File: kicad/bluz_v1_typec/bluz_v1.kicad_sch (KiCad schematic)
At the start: 73 parts, among them J10 Conn, J11 Conn, J12 BTAnt, J2 Conn, J3 Conn, J4 Conn, J5 Conn, J6 Conn, J7 Conn, J8 Conn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

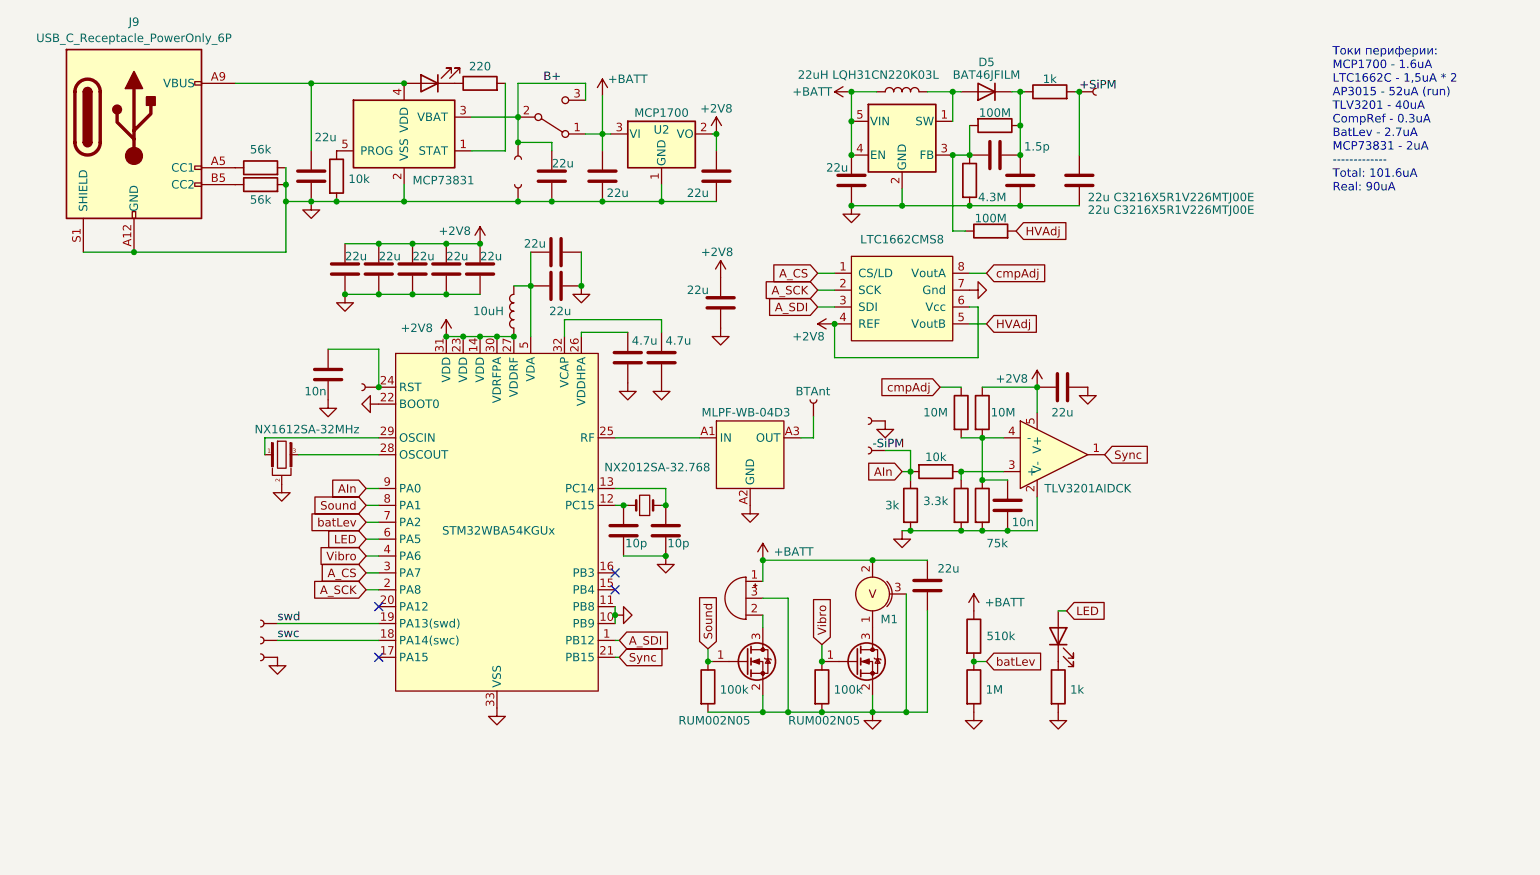
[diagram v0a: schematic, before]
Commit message: удалено:       kicad/bluz_v1_typec/bluz_v1-backups/bluz_v1-2024-12-26_190152.zip 	удалено:       kicad/bluz_v1_typec/bluz_v1-backups/bluz_v1-2024-12-27_152005.zip 	удалено:       kicad/bluz_v1_typec/bluz_v1-backups/bluz_v1-2025-01-20_122513.zip 	удалено:       kicad/bluz_v1_typec/bluz_v1-backups/bluz_v1-2025-01-21_100500.zip 	удалено:       kicad/bluz_v1_typec/bluz_v1-backups/bluz_v1-2025-01-21_105512.zip 	удалено:       kicad/bluz_v1_typec/bluz_v1-backups/bluz_v1-2025-01-21_110513.zip 	изменено:      kicad/bluz_v1_typec/bluz_v1.kicad_pcb 	изменено:      kicad/bluz_v1_typec/bluz_v1.kicad_pro 	изменено:      kicad/bluz_v1_typec/bluz_v1.kicad_sch 	изменено:      kicad/bluz_v1_typec/fp-info-cache
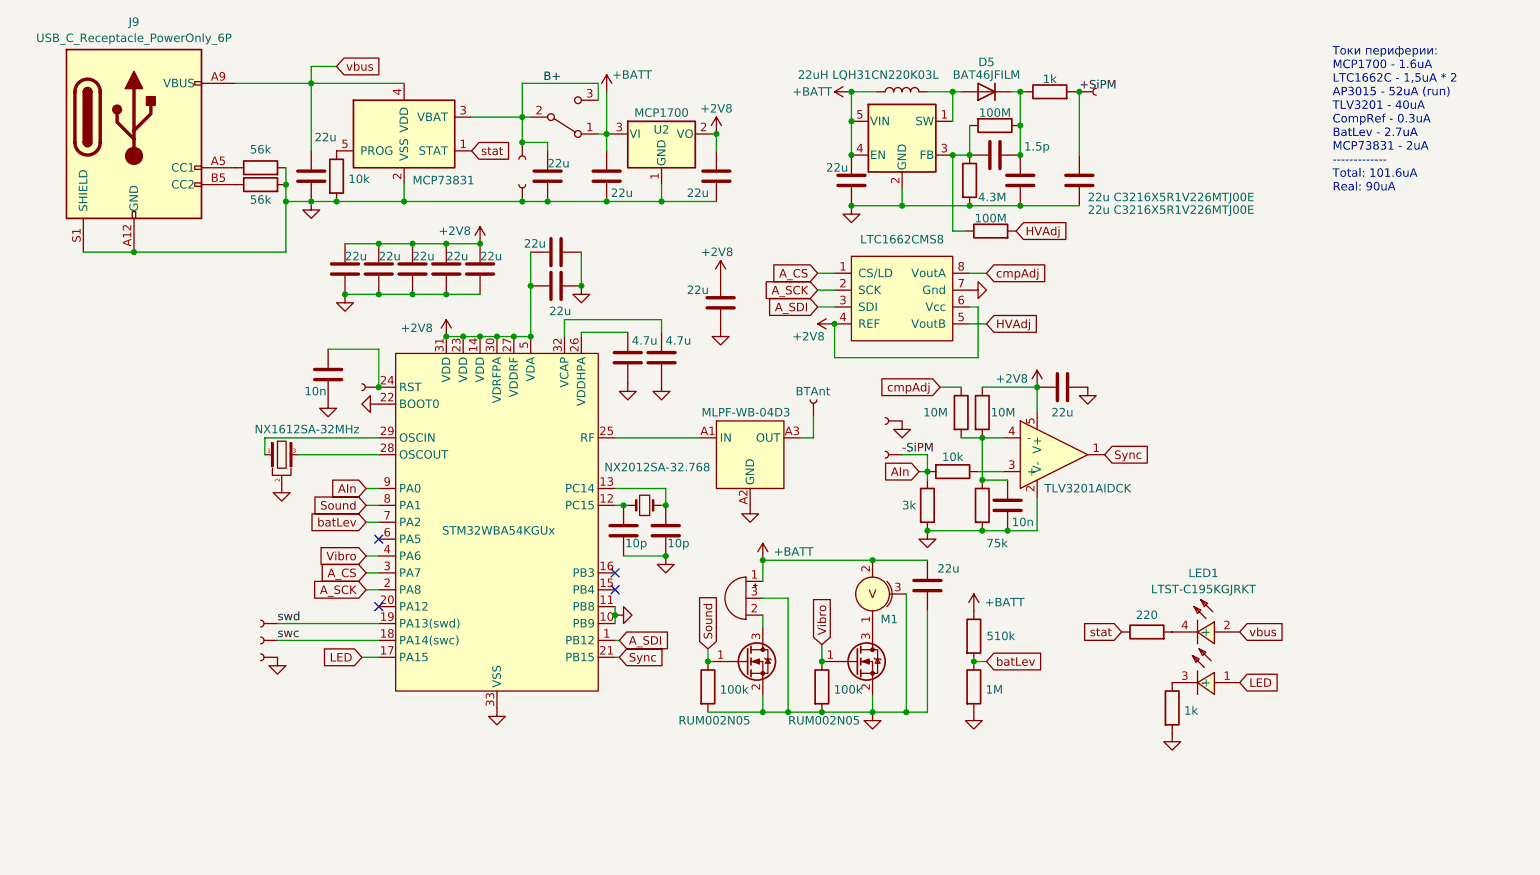
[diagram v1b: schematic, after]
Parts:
- removed D2: Red, LED_SMD:LED_0402_1005Metric, symbol Device:LED
- removed D3: Green, LED_SMD:LED_0402_1005Metric, symbol Device:LED
- removed L1: 10uH, Inductor_SMD:L_0603_1608Metric, symbol Device:L
- removed R*1: 3.3k, Resistor_SMD:R_0201_0603Metric, symbol Device:R
- added LED1: LTST-C195KGJRKT, easyeda2kicad:LED-ARRAY-SMD_0603-4P-L1.6-W1.5-BR-RD, symbol easyeda2kicad:LTST-C195KGJRKT
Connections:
- net +2V8: now also C23.1, C8.1, D1.5 (VDA)
- net LED: now also D1.17 (PA15), LED1.1 (+); no longer D1.6 (PA5)
- net stat: now reaches R4.1
- net stat: now also U1.1 (STAT)
- net at R4.2: now also LED1.4 (-); no longer U1.1 (STAT)
- net vbus: now reaches C4.1, J9.A9 (VBUS), J9.B9 (VBUS), U1.4 (VDD)
- net vbus: now also LED1.2 (+)
- net at R5.1: now also LED1.3 (-)

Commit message: удалено:       kicad/bluz_v1_typec/bluz_v1-backups/bluz_v1-2025-01-22_110710.zip 	удалено:       kicad/bluz_v1_typec/bluz_v1-backups/bluz_v1-2025-01-28_102500.zip 	удалено:       kicad/bluz_v1_typec/bluz_v1-backups/bluz_v1-2025-01-28_134021.zip 	удалено:       kicad/bluz_v1_typec/bluz_v1-backups/bluz_v1-2025-02-11_170038.zip 	удалено:       kicad/bluz_v1_typec/bluz_v1-backups/bluz_v1-2025-02-25_125512.zip 	изменено:      kicad/bluz_v1_typec/bluz_v1.kicad_pcb 	изменено:      kicad/bluz_v1_typec/bluz_v1.kicad_prl 	изменено:      kicad/bluz_v1_typec/bluz_v1.kicad_pro 	изменено:      kicad/bluz_v1_typec/bluz_v1.kicad_sch 	изменено:      kicad/bluz_v1_typec/fp-info-cache 	изменено:      kicad/bluz_v1_typec/gerber/BluZ.zip 	удалено:       kicad/bluz_v1_typec/gerber/bluz_v1-job.gbrjob 	изменено:      kicad/bluz_v1_typec/gerber/mk-gerber.sh 	изменено:      kicad/bluz_v1_typec/gerber/mk-gerber.sh~
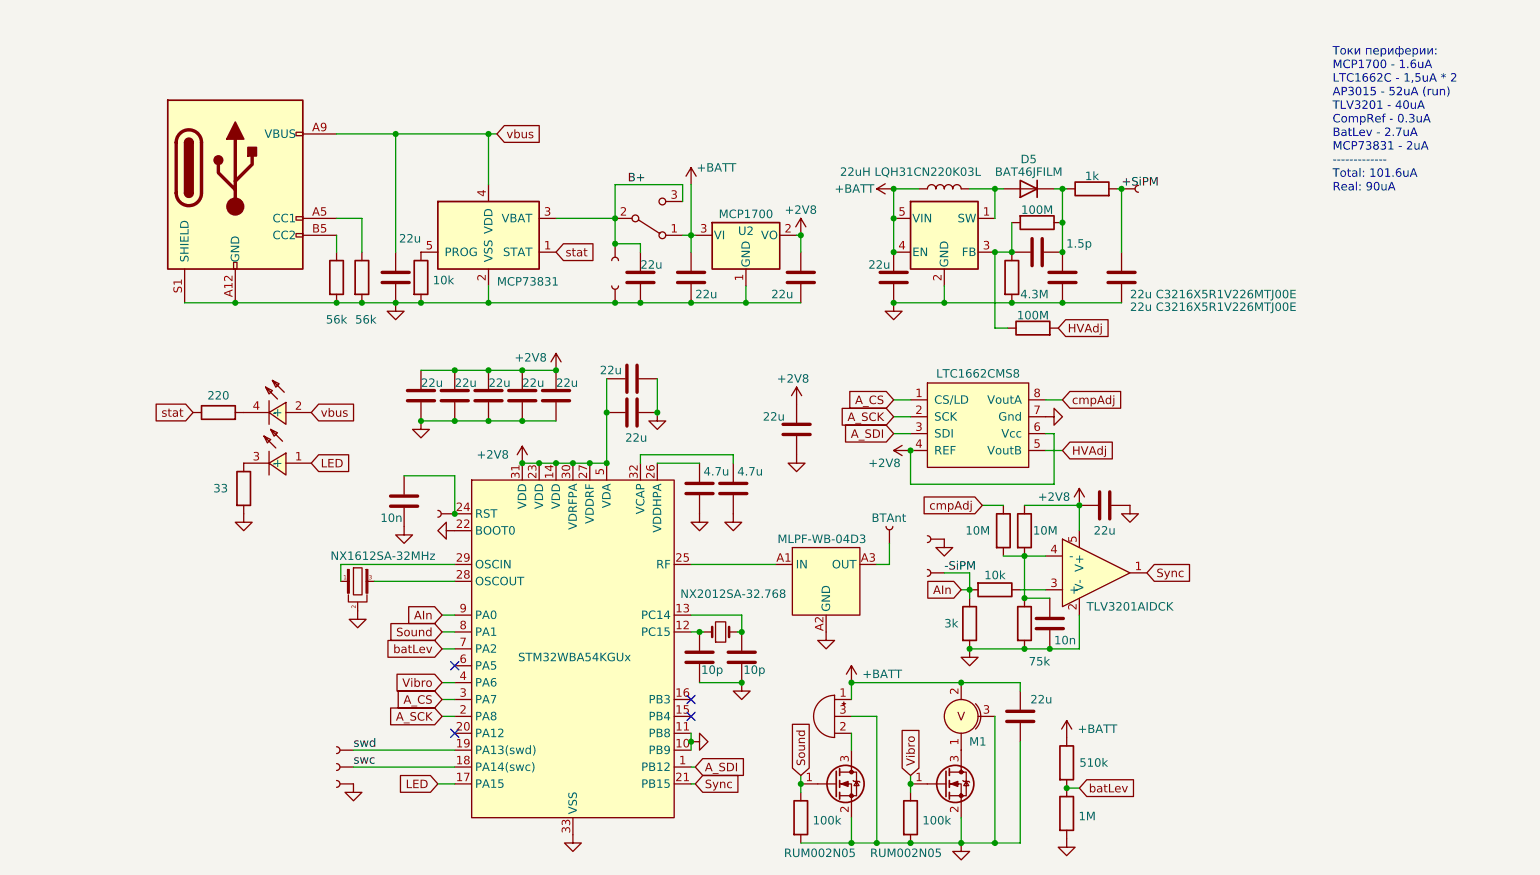
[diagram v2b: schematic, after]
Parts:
- removed BZ1: Buzzer, My-library:Buzzer55x55, symbol Device:Buzzer
- added BZ1: Buzzer, lib:Buzzer55x55, symbol My_Library:Buzzer
- R5: value 1k -> 33
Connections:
- net +BATT: now also BZ1.1 (-)
- net GND: now also BZ1.3 (GND)
- net at Q1.3 (D): now also BZ1.2 (+)
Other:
- moved on the sheet: D5, M1, U2

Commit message: удалено:       kicad/bluz_v1_typec/bluz_v1-backups/bluz_v1-2025-03-25_124207.zip 	удалено:       kicad/bluz_v1_typec/bluz_v1-backups/bluz_v1-2025-03-25_145630.zip 	изменено:      kicad/bluz_v1_typec/bluz_v1.kicad_pcb 	изменено:      kicad/bluz_v1_typec/bluz_v1.kicad_prl 	изменено:      kicad/bluz_v1_typec/bluz_v1.kicad_sch
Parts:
- R17, R18: value 56k -> 5.1k
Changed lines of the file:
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@@
 	(wire
 		(pts
-			(xy 69.85 125.73) (xy 85.09 125.73)
+			(xy 73.66 125.73) (xy 85.09 125.73)
 		)
 		(stroke
@@
 	(wire
 		(pts
-			(xy 82.55 128.27) (xy 85.09 128.27)
+			(xy 83.82 128.27) (xy 85.09 128.27)
 		)
 		(stroke
@@
 	(wire
 		(pts
-			(xy 69.85 123.19) (xy 85.09 123.19)
+			(xy 73.66 123.19) (xy 85.09 123.19)
 		)
 		(stroke
@@
 	(wire
 		(pts
-			(xy 83.185 107.95) (xy 85.09 107.95)
+			(xy 83.82 107.95) (xy 85.09 107.95)
 		)
 		(stroke
@@
 	(wire
 		(pts
-			(xy 83.185 102.87) (xy 85.09 102.87)
+			(xy 83.82 102.87) (xy 85.09 102.87)
 		)
 		(stroke
@@
 	(wire
 		(pts
-			(xy 83.185 118.11) (xy 85.09 118.11)
+			(xy 83.82 118.11) (xy 85.09 118.11)
 		)
 		(stroke
@@
 	(wire
 		(pts
-			(xy 83.185 113.03) (xy 85.09 113.03)
+			(xy 83.82 113.03) (xy 85.09 113.03)
 		)
 		(stroke
@@
 	(wire
 		(pts
-			(xy 83.185 115.57) (xy 85.09 115.57)
+			(xy 83.82 115.57) (xy 85.09 115.57)
 		)
 		(stroke
@@
 	(wire
 		(pts
-			(xy 83.185 105.41) (xy 85.09 105.41)
+			(xy 83.82 105.41) (xy 85.09 105.41)
 		)
 		(stroke
@@
 	)
 	(label "swd"
-		(at 69.85 123.19 0)
+		(at 73.66 123.19 0)
 		(effects
 			(font
@@
 	)
 	(label "swc"
-		(at 69.85 125.73 0)
+		(at 73.66 125.73 0)
 		(effects
 			(font
@@
 	(global_label "Vibro"
 		(shape input)
-		(at 83.185 113.03 180)
+		(at 83.82 113.03 180)
 		(fields_autoplaced yes)
 		(effects
@@
 		)
 		(property "Intersheetrefs" "${INTERSHEET_REFS}"
-			(at 75.9943 113.1094 0)
+			(at 76.6293 113.1094 0)
 			(effects
 				(font
@@
 	(global_label "A_SCK"
 		(shape input)
-		(at 83.185 118.11 180)
+		(at 83.82 118.11 180)
 		(fields_autoplaced yes)
 		(effects
@@
 		)
 		(property "Intersheetrefs" "${INTERSHEET_REFS}"
-			(at 74.9662 118.0306 0)
+			(at 75.6012 118.0306 0)
 			(effects
 				(font
@@
 	(global_label "AIn"
 		(shape input)
-		(at 83.185 102.87 180)
+		(at 83.82 102.87 180)
 		(fields_autoplaced yes)
 		(effects
@@
 		)
 		(property "Intersheetrefs" "${INTERSHEET_REFS}"
-			(at 77.9295 102.9494 0)
+			(at 78.5645 102.9494 0)
 			(effects
 				(font
@@
 	(global_label "Sound"
 		(shape input)
-		(at 83.185 105.41 180)
+		(at 83.82 105.41 180)
 		(fields_autoplaced yes)
 		(effects
@@
 		)
 		(property "Intersheetrefs" "${INTERSHEET_REFS}"
-			(at 74.9662 105.3306 0)
+			(at 75.6012 105.3306 0)
 			(effects
 				(font
@@
 	(global_label "A_CS"
 		(shape input)
-		(at 83.185 115.57 180)
+		(at 83.82 115.57 180)
 		(fields_autoplaced yes)
 		(effects
@@
 		)
 		(property "Intersheetrefs" "${INTERSHEET_REFS}"
-			(at 76.2362 115.4906 0)
+			(at 76.8712 115.4906 0)
 			(effects
 				(font
@@
 	(global_label "batLev"
 		(shape input)
-		(at 83.185 107.95 180)
+		(at 83.82 107.95 180)
 		(fields_autoplaced yes)
 		(effects
@@
 		)
 		(property "Intersheetrefs" "${INTERSHEET_REFS}"
-			(at 74.6638 108.0294 0)
+			(at 75.2988 108.0294 0)
 			(effects
 				(font
@@
 	(global_label "LED"
 		(shape input)
-		(at 82.55 128.27 180)
+		(at 83.82 128.27 180)
 		(fields_autoplaced yes)
 		(effects
@@
 		)
 		(property "Intersheetrefs" "${INTERSHEET_REFS}"
-			(at 76.6898 128.3494 0)
+			(at 77.9598 128.3494 0)
 			(effects
 				(font
@@
 			)
 		)
-		(property "Value" "56k"
+		(property "Value" "5.1k"
 			(at 67.31 58.42 0)
 			(effects
@@
 	(symbol
 		(lib_id "My-Library:Conn")
-		(at 67.31 128.27 180)
+		(at 71.12 128.27 180)
 		(unit 1)
 		(exclude_from_sim no)
@@
 		(fields_autoplaced yes)
 		(property "Reference" "J10"
-			(at 66.5988 129.1047 0)
+			(at 70.4088 129.1047 0)
 			(effects
 				(font
@@
 		)
 		(property "Value" "Conn"
-			(at 66.5988 126.5678 0)
+			(at 70.4088 126.5678 0)
 			(effects
 				(font
@@
 		)
 		(property "Footprint" "lib:conn_mini"
-			(at 66.04 124.46 0)
+			(at 69.85 124.46 0)
 			(effects
 				(font
@@
 		)
 		(property "Datasheet" "~"
-			(at 67.31 128.27 0)
+			(at 71.12 128.27 0)
 			(effects
 				(font
@@
 		)
 		(property "Description" ""
-			(at 67.31 128.27 0)
+			(at 71.12 128.27 0)
 			(effects
 				(font
@@
 	(symbol
 		(lib_id "My-Library:Conn")
-		(at 67.31 125.73 180)
+		(at 71.12 125.73 180)
 		(unit 1)
 		(exclude_from_sim no)
@@
 		(fields_autoplaced yes)
 		(property "Reference" "J5"
-			(at 66.5988 126.5647 0)
+			(at 70.4088 126.5647 0)
 			(effects
 				(font
@@
 		)
 		(property "Value" "Conn"
-			(at 66.5988 124.0278 0)
+			(at 70.4088 124.0278 0)
 			(effects
 				(font
@@
 		)
 		(property "Footprint" "lib:conn_mini"
-			(at 66.04 121.92 0)
+			(at 69.85 121.92 0)
 			(effects
 				(font
@@
 		)
 		(property "Datasheet" "~"
-			(at 67.31 125.73 0)
+			(at 71.12 125.73 0)
 			(effects
 				(font
@@
 		)
 		(property "Description" ""
-			(at 67.31 125.73 0)
+			(at 71.12 125.73 0)
 			(effects
 				(font
@@
 	(symbol
 		(lib_id "My-Library:Conn")
-		(at 67.31 123.19 180)
+		(at 71.12 123.19 180)
 		(unit 1)
 		(exclude_from_sim no)
@@
 		(fields_autoplaced yes)
 		(property "Reference" "J4"
-			(at 66.5988 124.0247 0)
+			(at 70.4088 124.0247 0)
 			(effects
 				(font
@@
 		)
 		(property "Value" "Conn"
-			(at 66.5988 121.4878 0)
+			(at 70.4088 121.4878 0)
 			(effects
 				(font
@@
 		)
 		(property "Footprint" "lib:conn_mini"
-			(at 66.04 119.38 0)
+			(at 69.85 119.38 0)
 			(effects
 				(font
@@
 		)
 		(property "Datasheet" "~"
-			(at 67.31 123.19 0)
+			(at 71.12 123.19 0)
 			(effects
 				(font
@@
 		)
 		(property "Description" ""
-			(at 67.31 123.19 0)
+			(at 71.12 123.19 0)
 			(effects
 				(font
@@
 	(symbol
 		(lib_id "power:GND")
-		(at 69.85 128.27 0)
+		(at 73.66 128.27 0)
 		(unit 1)
 		(exclude_from_sim no)
@@
 		(fields_autoplaced yes)
 		(property "Reference" "#PWR02"
-			(at 69.85 134.62 0)
+			(at 73.66 134.62 0)
 			(effects
 				(font
@@
 		)
 		(property "Value" "GND"
-			(at 69.85 132.7134 0)
+			(at 73.66 132.7134 0)
 			(effects
 				(font
@@
 		)
 		(property "Footprint" ""
-			(at 69.85 128.27 0)
+			(at 73.66 128.27 0)
 			(effects
 				(font
@@
 		)
 		(property "Datasheet" ""
-			(at 69.85 128.27 0)
+			(at 73.66 128.27 0)
 			(effects
 				(font
@@
 		)
 		(property "Description" ""
-			(at 69.85 128.27 0)
+			(at 73.66 128.27 0)
 			(effects
 				(font
@@
 			)
 		)
-		(property "Value" "56k"
+		(property "Value" "5.1k"
 			(at 70.104 58.42 0)
 			(effects

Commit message: изменено:      kicad/bluz_v1_typec/bluz_v1.kicad_pcb 	изменено:      kicad/bluz_v1_typec/bluz_v1.kicad_prl 	изменено:      kicad/bluz_v1_typec/bluz_v1.kicad_sch 	изменено:      stm32cubeide/BluZ_LPM/.mxproject 	изменено:      stm32cubeide/BluZ_LPM/BluZ_LPM.ioc 	изменено:      stm32cubeide/BluZ_LPM/Core/Inc/main.h 	изменено:      stm32cubeide/BluZ_LPM/Core/Src/main.c 	изменено:      stm32cubeide/BluZ_LPM/Release/BluZ_LPM.elf
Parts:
- D5: value BAT46JFILM -> BAS16
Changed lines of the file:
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@@
 			)
 		)
-		(property "Value" "BAT46JFILM"
+		(property "Value" "BAS16"
 			(at 171.45 36.195 0)
 			(effects

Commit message: удалено:       kicad/bluz_v1_typec/bluz_v1-backups/bluz_v1-2025-06-09_170559.zip 	удалено:       kicad/bluz_v1_typec/bluz_v1-backups/bluz_v1-2025-06-09_180824.zip 	удалено:       kicad/bluz_v1_typec/bluz_v1-backups/bluz_v1-2025-06-19_095726.zip 	удалено:       kicad/bluz_v1_typec/bluz_v1-backups/bluz_v1-2025-08-04_163535.zip 	изменено:      kicad/bluz_v1_typec/bluz_v1.kicad_pcb 	изменено:      kicad/bluz_v1_typec/bluz_v1.kicad_prl 	изменено:      kicad/bluz_v1_typec/bluz_v1.kicad_sch
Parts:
- R5: value 33 -> 82
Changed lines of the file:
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@@
 			)
 		)
-		(property "Value" "33"
+		(property "Value" "82"
 			(at 48.768 83.82 0)
 			(effects

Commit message: изменено:      Android/BluZ_LPM/BluZ/src/main/java/ru/starline/bluz/MainActivity.kt 	изменено:      kicad/bluz_v1_typec/bluz_v1.kicad_pcb 	изменено:      kicad/bluz_v1_typec/bluz_v1.kicad_sch
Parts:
- added C25, C26: 47n, Capacitor_SMD:C_0402_1005Metric, symbol Device:C
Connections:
- net +BATT: now also C25.1, C26.1
- net at BZ1.2 (+), Q1.3 (D): now also C25.2
- net at M1.1, Q2.3 (D): now also C26.2
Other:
- moved on the sheet: M1

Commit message: изменено:      kicad/bluz_v1_typec/bluz_v1.kicad_pcb 	изменено:      kicad/bluz_v1_typec/bluz_v1.kicad_sch 	изменено:      kicad/bluz_v1_typec/bom/ibom.html
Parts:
- BZ1: value Buzzer -> MLT-5020
- M1: value VibroMotor -> Z3OC1T8219731
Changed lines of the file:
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@@
 			)
 		)
-		(property "Value" "Buzzer"
+		(property "Value" "MLT-5020"
 			(at 141.478 113.8991 0)
 			(effects
@@
 			)
 		)
-		(property "Value" "VibroMotor"
+		(property "Value" "Z3OC1T8219731"
 			(at 166.37 116.8401 0)
 			(effects

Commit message: удалено:       kicad/bluz_v1_typec/bluz_v1-backups/bluz_v1-2025-08-04_173346.zip 	изменено:      kicad/bluz_v1_typec/bluz_v1.kicad_pcb 	изменено:      kicad/bluz_v1_typec/bluz_v1.kicad_sch 	изменено:      kicad/bluz_v1_typec/bom/ibom.html
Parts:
- D5: value BAS16 -> BAS16J
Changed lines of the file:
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@@
 			)
 		)
-		(property "Value" "BAS16"
+		(property "Value" "BAS16J"
 			(at 171.45 36.195 0)
 			(effects
